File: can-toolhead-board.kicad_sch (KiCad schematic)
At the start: 19 parts, among them J1 MF3-2x2P, U1 TPS62933, U2 MIC5365-3.3YC5

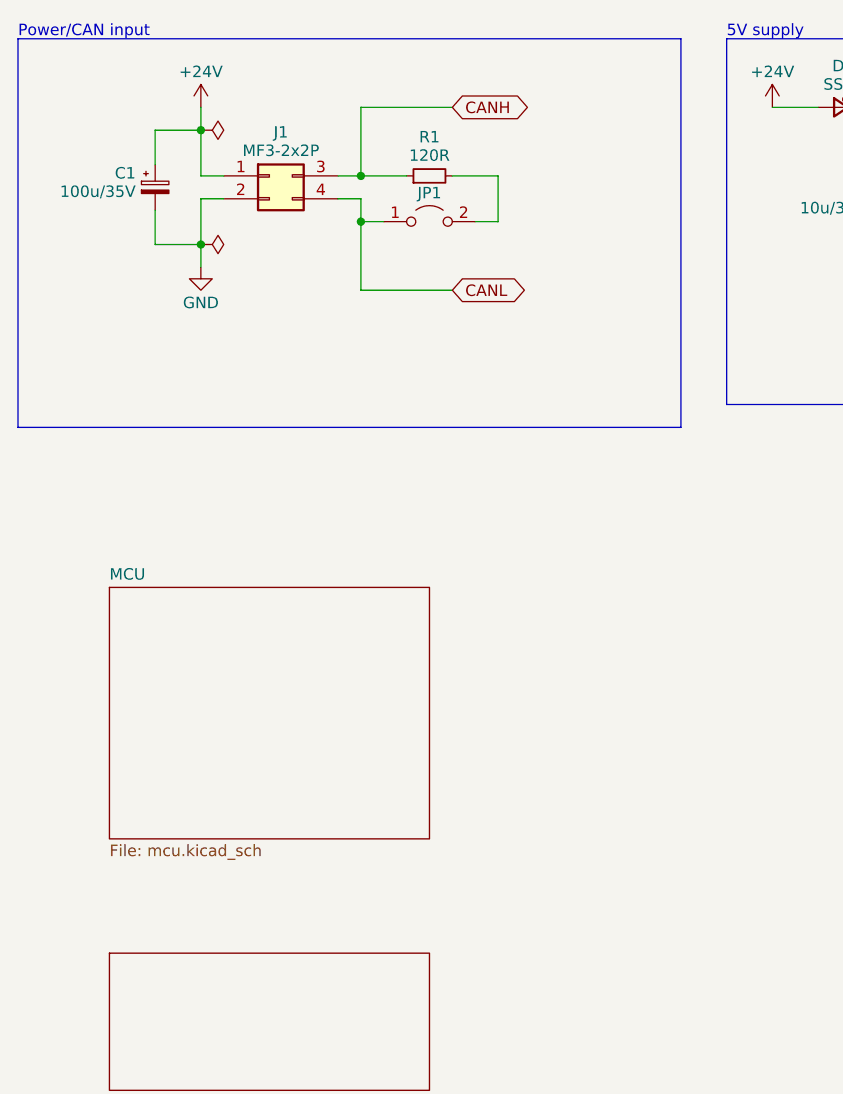
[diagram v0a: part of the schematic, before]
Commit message: Added solder jumpers for CAN/USB interface selection
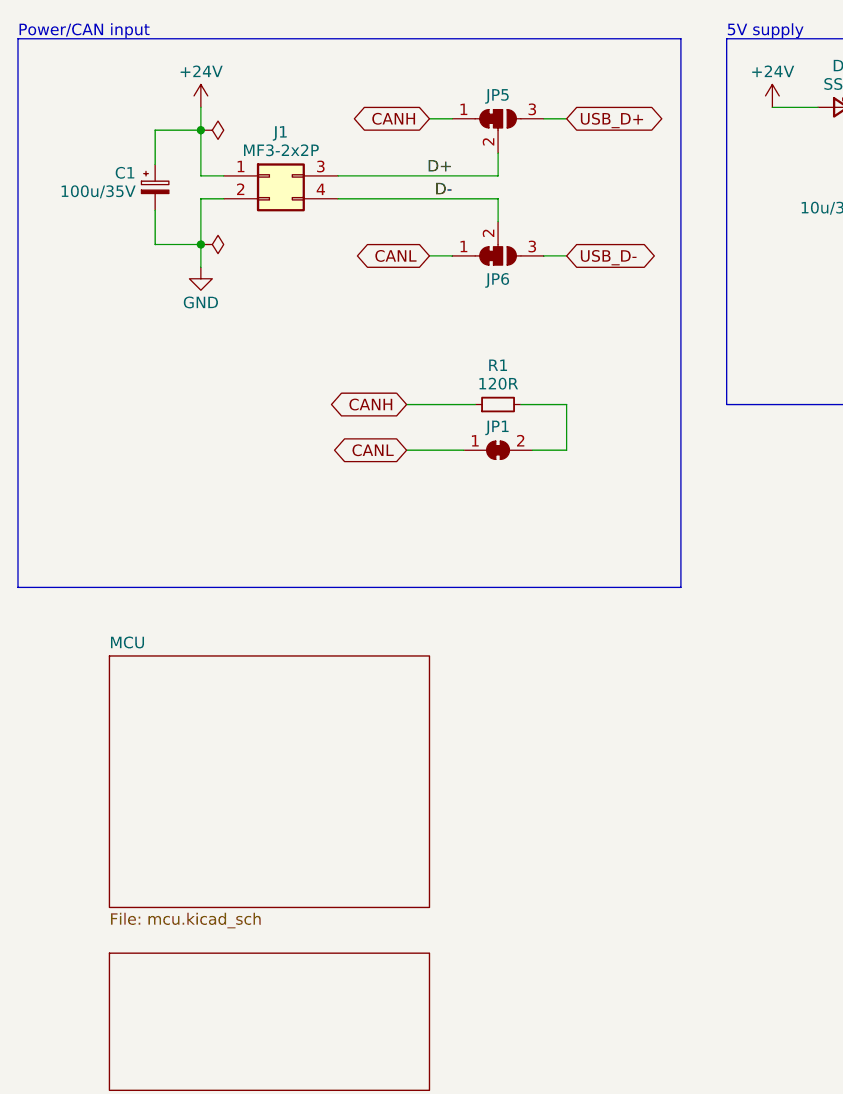
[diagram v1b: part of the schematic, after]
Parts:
- added JP5, JP6: SolderJumper_3_Bridged12, Jumper:SolderJumper-3_P1.3mm_Bridged12_RoundedPad1.0x1.5mm, symbol Jumper:SolderJumper_3_Bridged12
- JP1: footprint Connector_PinHeader_2.00mm:PinHeader_1x02_P2.00mm_Vertical -> Jumper:SolderJumper-2_P1.3mm_Bridged_RoundedPad1.0x1.5mm; symbol Jumper:Jumper_2_Open -> Jumper:SolderJumper_2_Bridged
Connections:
- net CANH: now also JP5.1 (A); no longer J1.3 (Pin_3)
- net CANL: now also JP6.1 (A); no longer J1.4 (Pin_4)
- new net D+: J1.3 (Pin_3), JP5.2 (C)
- new net D-: J1.4 (Pin_4), JP6.2 (C)
- new net USB_D+: JP5.3 (B)
- new net USB_D-: JP6.3 (B)
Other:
- moved on the sheet: R1

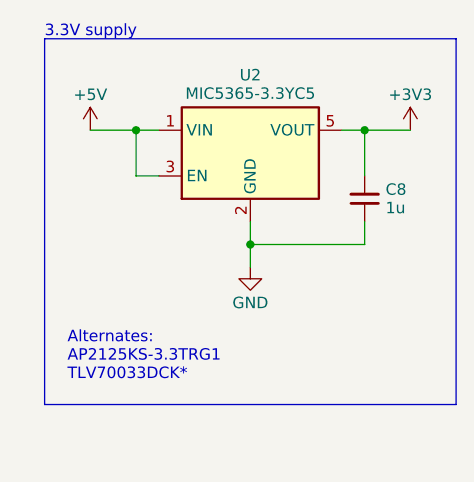
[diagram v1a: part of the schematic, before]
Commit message: Change 3V3 output cap to 4u7
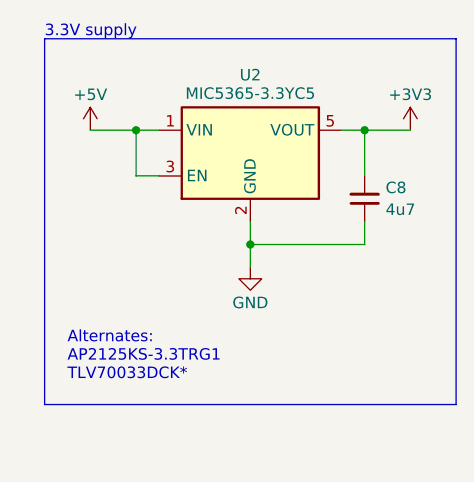
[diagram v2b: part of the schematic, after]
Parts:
- C8: value 1u -> 4u7; footprint Capacitor_SMD:C_0402_1005Metric -> Capacitor_SMD:C_0603_1608Metric; LCSC C52923 -> C19666
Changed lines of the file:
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@@
 		(fields_autoplaced yes)
 		(property "Reference" "C8"
-			(at 271.5641 39.6096 0)
+			(at 271.5641 39.4214 0)
 			(effects
 				(font
@@
 			)
 		)
-		(property "Value" "1u"
-			(at 271.5641 41.6576 0)
+		(property "Value" "4u7"
+			(at 271.5641 41.8457 0)
 			(effects
 				(font
@@
 			)
 		)
-		(property "Footprint" "Capacitor_SMD:C_0402_1005Metric"
+		(property "Footprint" "Capacitor_SMD:C_0603_1608Metric"
 			(at 269.24 40.64 0)
 			(effects
@@
 			)
 		)
-		(property "LCSC" "C52923"
+		(property "LCSC" "C19666"
 			(at 269.24 40.64 0)
 			(effects

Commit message: Add USB CC pulldown resistors
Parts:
- added C10, C11, C12: 0u1, Capacitor_SMD:C_0402_1005Metric, symbol Device:C_Small
- added C9: 10n, Capacitor_SMD:C_0402_1005Metric, symbol Device:C_Small
- added D2: DSS14, Diode_SMD:D_SOD-123F, symbol Device:D_Schottky_Small
- added J2: USB_C_Receptacle_USB2.0, Connector_USB:USB_C_Receptacle_GCT_USB4105-xx-A_16P_TopMnt_Horizontal, symbol Connector:USB_C_Receptacle_USB2.0_16P
- added J3: SH-6P, Connector_JST:JST_SH_SM06B-SRSS-TB_1x06-1MP_P1.00mm_Horizontal, symbol Connector_Generic:Conn_01x06
- added JP2: Jumper_2_Open, Connector_PinHeader_2.00mm:PinHeader_1x02_P2.00mm_Vertical, symbol Jumper:Jumper_2_Open
- added R4: 1M, Resistor_SMD:R_0402_1005Metric, symbol Device:R_Small
- added R5, R6: 5K1, Resistor_SMD:R_0402_1005Metric, symbol Device:R_Small
- added R7: 10K, Resistor_SMD:R_0402_1005Metric, symbol Device:R_Small
- added SW1, SW2: SW_Push, Button_Switch_SMD:SW_SPST_EVQP7A, symbol Switch:SW_Push
- added U3: TJA1051TK-3, Package_DFN_QFN:DFN-8-1EP_3x3mm_P0.65mm_EP1.55x2.4mm, symbol Interface_CAN_LIN:TJA1051TK-3
- added U4: STM32G0B1KBU6, Package_DFN_QFN:QFN-32-1EP_5x5mm_P0.5mm_EP3.45x3.45mm, symbol MCU_ST_STM32G0:STM32G0B1KBUx
- added U7: USBLC6-2P6, Package_TO_SOT_SMD:SOT-666, symbol Power_Protection:USBLC6-2P6
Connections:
- net +3V3: now also C12.1, J3.1 (Pin_1), R7.2, U3.5 (VIO), U4.4 (VDD)
- net +5V: now also C10.1, JP2.2 (B), U3.3 (VCC)
- net CANH: now also U3.7 (CANH)
- net CANL: now also U3.6 (CANL)
- net GND: now also C10.2, C11.2, C12.2, C9.2, J2.A1 (GND), J2.A12 (GND), J2.B1 (GND), J2.B12 (GND), J3.6 (Pin_6), R4.2, R5.2, R6.2, SW1.1, SW2.1, U3.2 (GND), U3.8 (S), U3.9 (GND), U4.33 (VSS), U4.5 (VSS), U7.2 (GND)
- net USB_D+: now also J2.A6 (D+), J2.B6 (D+), U4.23 (PA12/PA10), U7.6 (I/O1)
- net USB_D-: now also J2.A7 (D-), J2.B7 (D-), U4.22 (PA11/PA9), U7.4 (I/O2)
- new net: D2.1 (K), JP2.1 (A)
- new net: C9.1, J2.S1 (SHIELD), R4.1
- new net: J2.A5 (CC1), R5.1
- new net: J2.B5 (CC2), R6.1
- new net BOOT0: R7.1, SW2.2, U4.25 (PA14)
- new net CAN_RX: U3.4 (RXD), U4.15 (PB0)
- new net CAN_TX: U3.1 (TXD), U4.16 (PB1)
- new net HE: U4.10 (PA3)
- new net HEFAN: U4.8 (PA1)
- new net HEFAN_SENSE: U4.3 (PC15)
- new net MISO: J3.4 (Pin_4), U4.28 (PB4)
- new net MOSI: J3.3 (Pin_3), U4.29 (PB5)
- new net MOT_DIAG: U4.2 (PC14)
- new net MOT_DIR: U4.30 (PB6)
- new net MOT_STEP: U4.32 (PB8)
- new net MOT_UART: U4.31 (PB7)
- new net MOT_~{EN}: U4.1 (PB9)
- new net PCFAN: U4.7 (PA0)
- new net PROBE: U4.20 (PC6)
- new net RGB: U4.9 (PA2)
- new net SCK: J3.5 (Pin_5), U4.27 (PB3)
- new net STP0: U4.19 (PA9/UCPD1_DBCC1)
- new net STP1: U4.18 (PA8)
- new net STP2: U4.17 (PB2)
- new net SWDIO: U4.24 (PA13)
- new net TH0: U4.12 (PA5)
- new net TH1: U4.13 (PA6)
- new net VBUS: D2.2 (A), J2.A4 (VBUS), J2.A9 (VBUS), J2.B4 (VBUS), J2.B9 (VBUS), U7.5 (VBUS)
- new net ~{RST}: C11.1, SW1.2, U4.6 (PF2)
- new net ~{SS}: J3.2 (Pin_2), U4.26 (PA15)
- no-connect marks 1 -> 9
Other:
- removed sheet MCU
- note added: "CAN"
- note added: "PD"
- note added: "Power/CAN port"
- note added: "USB"
- note removed: "Power/CAN input"
- moved on the sheet: H1, H2, JP1, R1

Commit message: Add 3D models
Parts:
- J1: MPN (none) -> 43045-0400
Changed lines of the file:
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@@
 			)
 		)
-		(property "MPN" ""
+		(property "MPN" "43045-0400"
 			(at 50.8 38.1 0)
 			(effects

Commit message: Fix part LCSC ref
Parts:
- R6: LCSC C423253 -> C25905
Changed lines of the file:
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@@
 			)
 		)
-		(property "LCSC" "C423253"
+		(property "LCSC" "C25905"
 			(at 68.58 139.7 0)
 			(effects

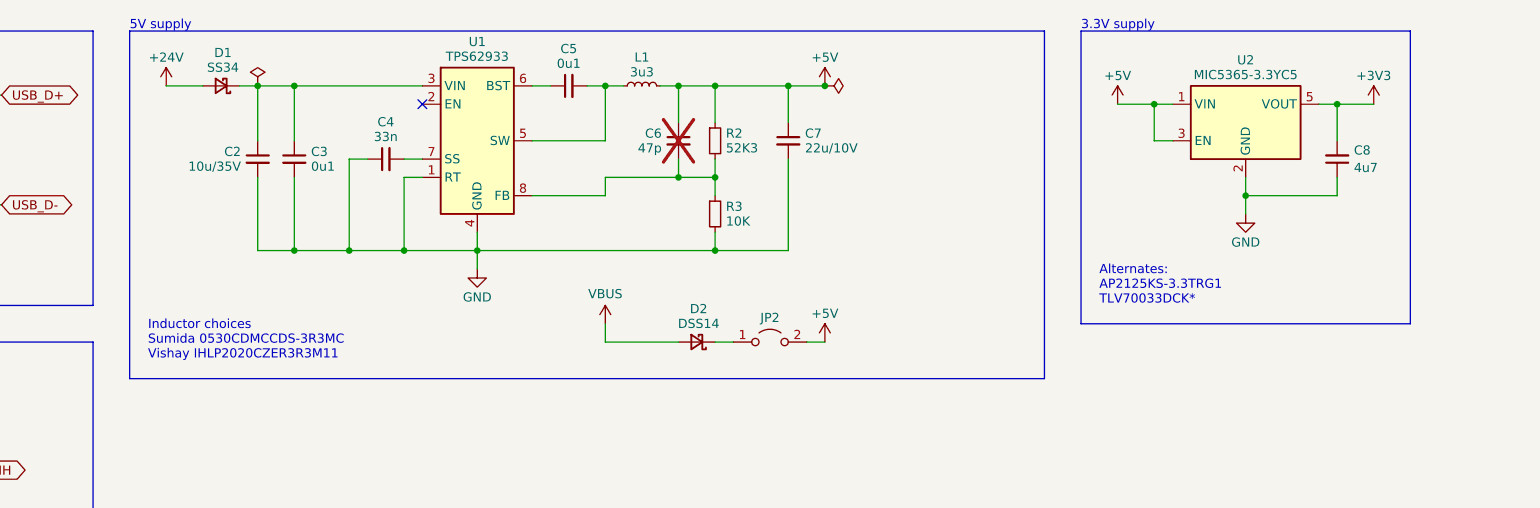
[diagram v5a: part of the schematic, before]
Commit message: Change 10uF cap on 24V input to 0805; change 33nF to 22nF to simplify BOM; add green power LED
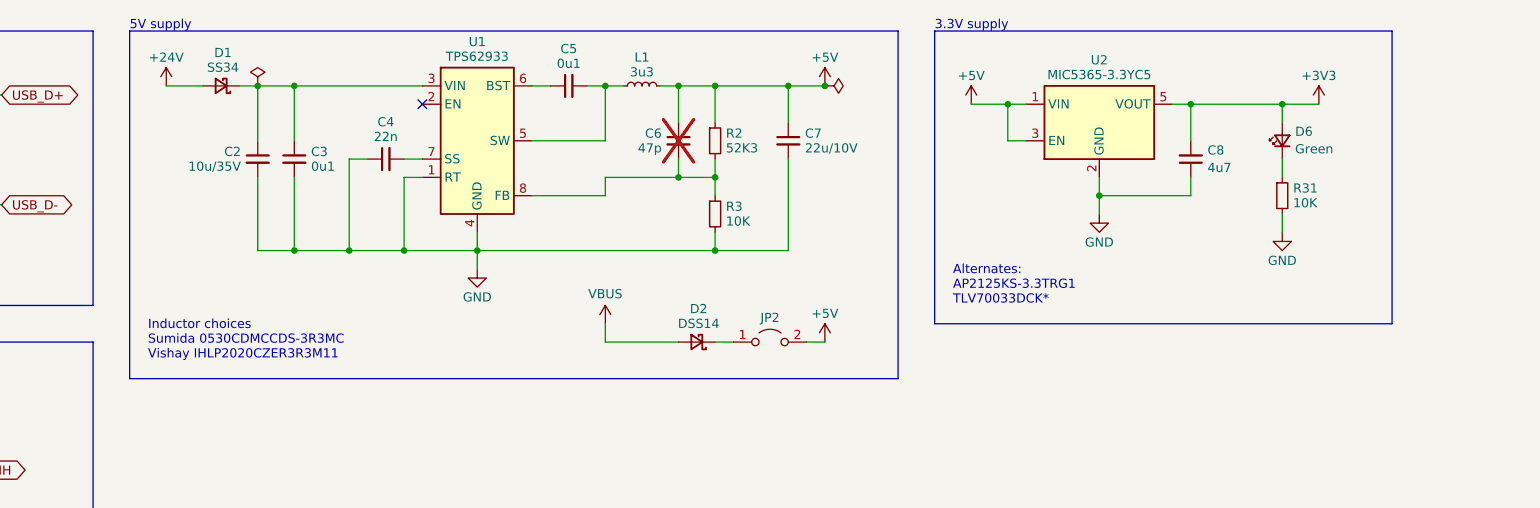
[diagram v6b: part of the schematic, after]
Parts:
- added D6: Green, LED_SMD:LED_0603_1608Metric, symbol Device:LED_Small
- added R31: 10K, Resistor_SMD:R_0402_1005Metric, symbol Device:R_Small
- C2: footprint Capacitor_SMD:C_0603_1608Metric -> Capacitor_SMD:C_0805_2012Metric; LCSC (none) -> C440198
- C4: value 33n -> 22n; LCSC C472437 -> C1532
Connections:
- net +3V3: now also D6.2 (A)
- net GND: now also R31.2
- new net: D6.1 (K), R31.1
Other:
- moved on the sheet: C8, U2

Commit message: Lots of little tweaks and simplifications
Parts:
- D6: LCSC (none) -> C12624
- J2: LCSC (none) -> C165948; MPN (none) -> TYPE-C-31-M-12
- J3: LCSC C161598 -> C160405
- JP1: value Jumper_2_Open -> SolderJumper_2_Bridged
- JP2: LCSC (none) -> C706997
- R4: value 1M -> 100K; LCSC C423253 -> C25741
- U3: LCSC (none) -> C2875699
- U4: LCSC (none) -> C5159549; MPN (none) -> STM32G0B1KBU6
- U7: LCSC (none) -> C15999; MPN (none) -> USBLC6-2P6
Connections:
- net CANH: now also JP1.1 (A); no longer R1.1
- net CANL: now also R1.1; no longer JP1.1 (A)
- net PROBE: now also U4.21 (PA10/UCPD1_DBCC2); no longer U4.20 (PC6)
- net USB_D+: now also U7.4 (I/O2); no longer U7.6 (I/O1)
- net USB_D-: now also U7.6 (I/O1); no longer U7.4 (I/O2)
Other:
- note added: "MCU"
- note added: "Matching USB connectors: Amphenol 12402012E212A GCT USB4105-GF-A HRO TYPE-C-31-M-12 G-Switch GT-USB-7010ASV XKB U263-16XN-4XS1735 and more..."
- note added: "SPI port"
- note added: "UCPD1_CC1"
- note removed: "PD"
- moved on the sheet: C11, C12, H1, H2, J3, JP1, R1, R5, R6, R7, SW1, SW2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

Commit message: Modify SPI connector pinout
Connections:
- net GND: now also J3.2 (Pin_2); no longer J3.6 (Pin_6)
- net MOSI: now also J3.5 (Pin_5); no longer J3.3 (Pin_3)
- net SCK: now also J3.6 (Pin_6); no longer J3.5 (Pin_5)
- net ~{SS}: now also J3.3 (Pin_3); no longer J3.2 (Pin_2)
